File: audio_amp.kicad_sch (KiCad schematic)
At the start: 74 parts, among them IC115 RC4558, IC116 RC4558, IC117 RC4558, IC119 M51131L, IC120 CD4053B, P2 Conn_01x07_Male

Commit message: PCE expansion port added with only relevant pins.
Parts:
- removed #2: Conn_01x03_Female, symbol Connector:Conn_01x03_Female
- added #1, #5, L_#2, R_#2: Jumper_2_Bridged, symbol Jumper:Jumper_2_Bridged
- added C11: 100u, symbol Device:C_Polarized
- added C9: 100n, symbol Device:C
- added R120: 270, symbol Device:R
- added R35: 1k, symbol Device:R
- added R9: 75, symbol Device:R
- added SPC-E: PCE-EXPANSION-CONN, symbol IFU-30:PCE-EXPANSION-CONN
- added TR5: C2785, symbol Device:Q_NPN_ECB
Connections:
- net 7.9V: now also R120.1
- net GND: now also C11.2, C9.1, R9.2
- net PCE_AUDIO_LEFT: now also L_#2.1 (A), SPC-E.A0 (SNDL); no longer R14.1
- net PCE_AUDIO_RIGHT: now also R_#2.1 (A), SPC-E.C0 (SNDR); no longer R18.1
- net SPCE_B1_SNDIN renamed PCE_AUDIO_IN
- net PCE_AUDIO_IN: now also SPC-E.B0 (SNDIN)
- net VIDEO_IN: no longer names the net of C58.1
- net VIDEO_IN: now also #1.2 (B)
- new net: L_#2.2 (B), R14.1
- new net: #1.1 (A), R9.1, TR5.1 (E)
- new net: #5.1 (A), R120.2
- new net: R18.1, R_#2.2 (B)
- new net: #5.2 (B), C11.1, C9.2, TR5.2 (C)
- new net: R35.1, TR5.3 (B)
- new net PCE_VID: R35.2, SPC-E.A22 (VID)
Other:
- moved on the sheet: C12, C58, C8, IC117A, R104, R11, R15, R16, R21, R22, R33, R37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

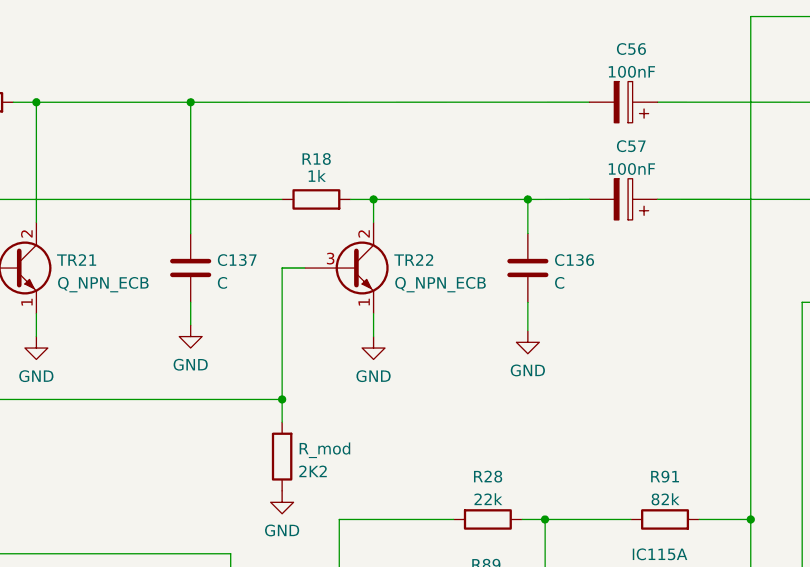
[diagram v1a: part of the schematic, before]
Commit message: Fixed mistake in ADPCM page and added notes about opamps.
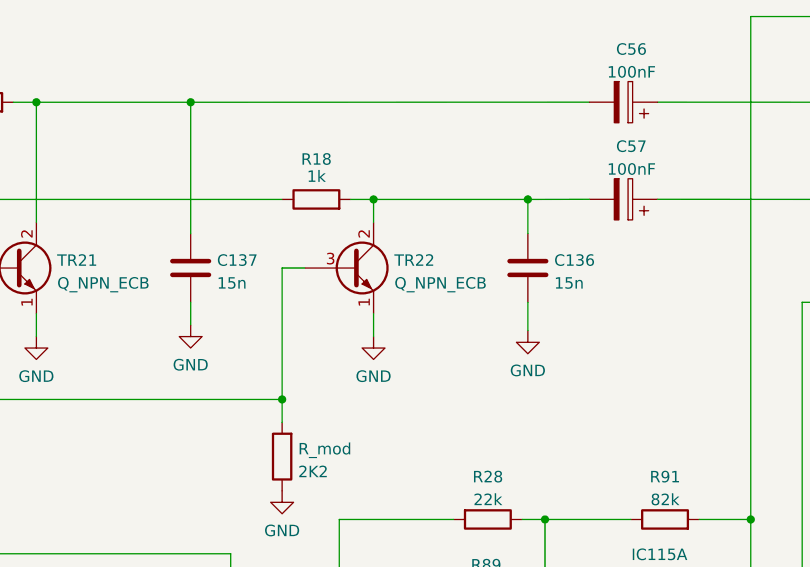
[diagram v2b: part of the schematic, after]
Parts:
- C136, C137: value C -> 15n
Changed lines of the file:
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@@
       (effects (font (size 1.27 1.27)) (justify left))
     )
-    (property "Value" "C" (id 1) (at 181.991 114.0972 0)
+    (property "Value" "15n" (id 1) (at 181.991 114.0972 0)
       (effects (font (size 1.27 1.27)) (justify left))
     )
@@
       (effects (font (size 1.27 1.27)) (justify left))
     )
-    (property "Value" "C" (id 1) (at 219.456 114.0972 0)
-      (effects (font (size 1.27 1.27)) (justify left))
-    )
+    (property "Value" "15n" (id 1) (at 219.456 114.0972 0)
+      (effects (font (size 1.27 1.27)) (justify left))
+    )

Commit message: All calculations added.
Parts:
- R91, R92: value 82k -> 8.2k
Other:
- note added: "text to paste into https://latex2png.com/ to have nice equations IC115A and B calculations At DC level \frac{V_{BIAS}/(15k+22k) + V_{BIAS}/28k + V_{IFU_R}/82k} {1/(15k+22k) + 1/28k + 1/8.2k}= V_{BIAS} \\ V_{BIAS}/37k + V_{BIAS}/28k + V_{IFU_R}/8.2k = V_{BIAS}/5.4144k \\ V_{IFU_R} = 3.95 \times (1/5.4144k - 1/37k - 1/28k) \times 8.2k \\ V_{IFU_R} = 3.95V V_{IFU_L} = 3.95V At AC level \frac{V_{CD_L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"
- note added: "text to paste into https://latex2png.com/ to have nice equations IC116A & IC116B calculations At DC level \frac{V_{IFUL}/R32 + V_{BIAS}/(R118+R31) + V_{AUDIOL}/R93}{1/R32 + 1/(R118+R31) + 1/R93} = V_{BIAS} \\ \frac{3.95/22k + 3.95/(15k+22k) + V_{AUDIOL}/62k} = 3.95 \times (1/22k + 1/(15k+22k) + 1/62) \\ V_{AUDIOL} = 62k \times 3.95 \times (1/11.285k - 1/22K - 1/37K) \\ V_{IFULR} = 3.95V At AC lev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"
- note added: "text to paste into https://latex2png.com/ to have nice equations V_{BIAS} = \frac{R20}{R20 + R19} \times (9V - V_{D1} - V_{TR2 BE}) \\ V_{BIAS} = \frac{10k}{10k + 10k} \times 7.9 \\ V_{BIAS} = 1/2 \times 7.9 \\ V_{BIAS} = 3.95V IC117A calculations At DC level \frac{V_{IFUL}/R16 + V_{IFUR}/R22 + V_{IFULR}/R21}{1/R16 + 1/R22 + 1/R21} = V_{BIAS} \\ \frac{3.95/33k + 3.95/33k + V_{IFULR}/39k}{1/33k + 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"
- note removed: "text to paste into https://latex2png.com/ to have nice equations V_{BIAS} = \frac{R20}{R20 + R19} \times (9V - V_{D1} - V_{TR2 BE}) \\ V_{BIAS} = \frac{10k}{10k + 10k} \times 7.9 \\ V_{BIAS} = 1/2 \times 7.9 \\ V_{BIAS} = 3.95V V_{BIAS} = \frac{V_{IFUL}/R16 + V_{IFUR}/R22 + V_{IFULR}/R21}{1/R16 + 1/R22 + 1/R21} 3.95 = \frac{V_{IFUL}/33k + V_{IFUR}/33K + V_{IFULR}/39K}{1/33k + 1/33k + 1/39k} 13.29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"
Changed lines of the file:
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@@
     (effects (font (size 1.27 1.27)) (justify left bottom))
   )
-  (text "text to paste into https://latex2png.com/ to have nice equations\n\nV_{BIAS} = \\frac{R20}{R20 + R19} \\times (9V - V_{D1} - V_{TR2 BE}) \\\\\nV_{BIAS} = \\frac{10k}{10k + 10k} \\times 7.9 \\\\\nV_{BIAS} = 1/2 \\times 7.9 \\\\\nV_{BIAS} = 3.95V\n\nV_{BIAS} = \\frac{V_{IFUL}/R16 + V_{IFUR}/R22 + V_{IFULR}/R21}{1/R16 + 1/R22 + 1/R21}\n\n3.95 = \\frac{V_{IFUL}/33k + V_{IFUR}/33K + V_{IFULR}/39K}{1/33k + 1/33k + 1/39k}\n\n13.29 = V_{IFUL} \\times 39k/33k + V_{IFUR} \\times 39k/33K + V_{IFULR}\n\nV_{IFULR} = 13.29 - V_{IFUR} \\times 39k/33K - V_{IFUR} \\times 39k/33K\n\nV_{IFULR} = 13.29 - V_{IFUR} \\times 1.18 - V_{IFUR} \\times 1.18\n\n\n"
-    (at 234.95 259.715 0)
+  (text "text to paste into https://latex2png.com/ to have nice equations\n\nV_{BIAS} = \\frac{R20}{R20 + R19} \\times (9V - V_{D1} - V_{TR2 BE}) \\\\\nV_{BIAS} = \\frac{10k}{10k + 10k} \\times 7.9 \\\\\nV_{BIAS} = 1/2 \\times 7.9 \\\\\nV_{BIAS} = 3.95V\n\nIC117A calculations\n\nAt DC level\n\\frac{V_{IFUL}/R16 + V_{IFUR}/R22 + V_{IFULR}/R21}{1/R16 + 1/R22 + 1/R21} = V_{BIAS} \\\\\n\\frac{3.95/33k + 3.95/33k + V_{IFULR}/39k}{1/33k + 1/33k + 1/39k} = 3.95 \\\\\nV_{IFULR} = 39k \\times 3.95 \\times (1/11.595k - 1/33K - 1/33K) \\\\\nV_{IFULR} = 3.95V\n\nAt AC level\n\\frac{V_{IFUL}/R16 + V_{IFUR}/R22 + V_{IFULR}/R21}{1/R16 + 1/R22 + 1/R21} = 0 \\\\\nV_{IFUL}/R16 + V_{IFUR}/R22 + V_{IFULR}/R21 = 0 \\\\\nV_{IFUL}/33k + V_{IFUR}/33k + V_{IFULR}/39k = 0 \\\\\nV_{IFULR} = - V_{IFUR} \\times 39/33 - V_{IFUR} \\times 39/33\n\nGain is 39/33 = 1.18"
+    (at 231.14 256.54 0)
     (effects (font (size 1.27 1.27)) (justify left bottom))
   )
@@
     (effects (font (size 1.27 1.27)) (justify left bottom))
   )
+  (text "text to paste into https://latex2png.com/ to have nice equations\n\nIC116A & IC116B calculations\n\nAt DC level\n\\frac{V_{IFUL}/R32 + V_{BIAS}/(R118+R31) + V_{AUDIOL}/R93}{1/R32 + 1/(R118+R31) + 1/R93} = V_{BIAS} \\\\\n\\frac{3.95/22k + 3.95/(15k+22k) + V_{AUDIOL}/62k} = 3.95 \\times (1/22k + 1/(15k+22k) + 1/62) \\\\\nV_{AUDIOL} = 62k \\times 3.95 \\times (1/11.285k - 1/22K - 1/37K) \\\\\nV_{IFULR} = 3.95V\n\nAt AC level\n\\frac{V_{IFUL}/R32 + V_{PCEL}/R31 + V_{AUDIOL}/R93}{1/R32 + 1/R31 + 1/R93} = 0 \\\\\nV_{IFUL}/R32 + V_{PCEL}/R31 + V_{AUDIOL}/R93 = 0 \\\\\nV_{AUDIOL} = - R93 \\times (V_{IFUL}/R32 + V_{PCEL}/R31) \\\\\nV_{AUDIOL} = - V_{IFUL} \\times 62/22 - V_{PCEL} \\times 62/22 \\\\\n\nGain is 62/22 = 2.818\n\nMultiplied by previous gain, we get 8.2/22 * 62/22 = 1.05 close enough to 1 (by 5%)"
+    (at 250.825 63.5 0)
+    (effects (font (size 1.27 1.27)) (justify left bottom))
+  )
   (text "Note on transistors:\nA1175 = PNP\nA144 = PNP (re-biased)\nC2001 = NPN\nAIL3Z = NPN\nC2785 = NPN\n\n"
-    (at 240.03 54.61 0)
+    (at 168.91 33.655 0)
     (effects (font (size 1.27 1.27)) (justify left bottom))
   )
   (text "With control (P12) connected to REF (5.2V),\nVolume 1 is applied to both left and right\n(simultaneous volume mode)\nVolume 2 is actually balance control but is fixed to Vref/2 which makes L and R volumes even."
     (at 44.45 219.075 0)
+    (effects (font (size 1.27 1.27)) (justify left bottom))
+  )
+  (text "text to paste into https://latex2png.com/ to have nice equations\n\nIC115A and B calculations\n\nAt DC level\n\\frac{V_{BIAS}/(15k+22k) + V_{BIAS}/28k + V_{IFU_R}/82k} {1/(15k+22k) + 1/28k + 1/8.2k}= V_{BIAS} \\\\\nV_{BIAS}/37k + V_{BIAS}/28k + V_{IFU_R}/8.2k = V_{BIAS}/5.4144k \\\\\nV_{IFU_R} = 3.95 \\times (1/5.4144k - 1/37k - 1/28k) \\times 8.2k \\\\\nV_{IFU_R} = 3.95V\n\nV_{IFU_L} = 3.95V\n\nAt AC level\n\\frac{V_{CD_L}/22k + V_{ADPCM}/28k + V_{FADE_L}/22k + V_{IFU_L}/8.2k}{1/22k + 1/28k + 1/22k + 1/8.2k} = 0 \\\\\nV_{IFU_L} = 8.2k \\times (-V_{CD_L}/22k - V_{ADPCM}/28k - V_{FADE_L}/22k) \\\\\nV_{IFU_L} = - V_{CD_L} \\times 8.2/22 - V_{ADPCM} \\times 8.2/28 - V_{FADE_L} \\times 8.2/22 \\\\\n\nV_{IFU_R} = - V_{CD_R} \\times 8.2/22 - V_{ADPCM} \\times 8.2/28 - V_{FADE_R} \\times 8.2/22 \\\\\n\nGain is 8.2/22 = 0.373"
+    (at 117.475 269.24 0)
     (effects (font (size 1.27 1.27)) (justify left bottom))
   )
@@
     (in_bom yes) (on_board yes) (fields_autoplaced)
     (property "Reference" "R91" (id 0) (at 231.775 135.6192 90))
-    (property "Value" "82k" (id 1) (at 231.775 138.1561 90))
+    (property "Value" "8.2k" (id 1) (at 231.775 138.1561 90))
     (property "Footprint" "" (id 2) (at 231.775 142.113 90)
       (effects (font (size 1.27 1.27)) hide)
@@
     (in_bom yes) (on_board yes) (fields_autoplaced)
     (property "Reference" "R92" (id 0) (at 229.235 168.0042 90))
-    (property "Value" "82k" (id 1) (at 229.235 170.5411 90))
+    (property "Value" "8.2k" (id 1) (at 229.235 170.5411 90))
     (property "Footprint" "" (id 2) (at 229.235 174.498 90)
       (effects (font (size 1.27 1.27)) hide)

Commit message: Documentation started.
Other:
- title: (none) -> NEC PC-Engine IFU-30
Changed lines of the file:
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@@
 (kicad_sch (version 20211123) (generator eeschema)
   (paper "A3")
+  (title_block
+    (title "NEC PC-Engine IFU-30")
+    (date "2022-10-27")
+    (rev "0.1")
+    (comment 1 "Author: Regis Galland")
+    (comment 2 "NEC IFU-30 PCB reverse engineered schematics")
+  )
   (junction (at 59.055 172.72) (diameter 0) (color 0 0 0 0)
   )
@@
     (effects (font (size 1.27 1.27)) (justify left bottom))
   )
-  (text "text to paste into https://latex2png.com/ to have nice equations\n\nIC115A and B calculations\n\nAt DC level\n\\frac{V_{BIAS}/(15k+22k) + V_{BIAS}/28k + V_{IFU_R}/82k} {1/(15k+22k) + 1/28k + 1/8.2k}= V_{BIAS} \\\\\nV_{BIAS}/37k + V_{BIAS}/28k + V_{IFU_R}/8.2k = V_{BIAS}/5.4144k \\\\\nV_{IFU_R} = 3.95 \\times (1/5.4144k - 1/37k - 1/28k) \\times 8.2k \\\\\nV_{IFU_R} = 3.95V\n\nV_{IFU_L} = 3.95V\n\nAt AC level\n\\frac{V_{CD_L}/22k + V_{ADPCM}/28k + V_{FADE_L}/22k + V_{IFU_L}/8.2k}{1/22k + 1/28k + 1/22k + 1/8.2k} = 0 \\\\\nV_{IFU_L} = 8.2k \\times (-V_{CD_L}/22k - V_{ADPCM}/28k - V_{FADE_L}/22k) \\\\\nV_{IFU_L} = - V_{CD_L} \\times 8.2/22 - V_{ADPCM} \\times 8.2/28 - V_{FADE_L} \\times 8.2/22 \\\\\n\nV_{IFU_R} = - V_{CD_R} \\times 8.2/22 - V_{ADPCM} \\times 8.2/28 - V_{FADE_R} \\times 8.2/22 \\\\\n\nGain is 8.2/22 = 0.373"
-    (at 117.475 269.24 0)
+  (text "text to paste into https://latex2png.com/ to have nice equations\n\nIC115A and B calculations\n\nAt DC level\n\\frac{V_{BIAS}/(15k+22k) + V_{BIAS}/28k + V_{IFU_R}/82k} {1/(15k+22k) + 1/28k + 1/8.2k}= V_{BIAS} \\\\\nV_{BIAS}/37k + V_{BIAS}/28k + V_{IFU_R}/8.2k = V_{BIAS}/5.4144k \\\\\nV_{IFU_R} = 3.95 \\times (1/5.4144k - 1/37k - 1/28k) \\times 8.2k \\\\\nV_{IFU_R} = 3.95V\n\nV_{IFU_L} = 3.95V\n\nAt AC level\n\\frac{V_{CD_L}/22k + V_{ADPCM}/28k + V_{FADE_L}/22k + V_{IFU_L}/8.2k}{1/22k + 1/28k + 1/22k + 1/8.2k} = 0 \\\\\nV_{IFU_L} = 8.2k \\times (-V_{CD_L}/22k - V_{ADPCM}/28k - V_{FADE_L}/22k) \\\\\nV_{IFU_L} = - V_{CD_L} \\times 8.2/22 - V_{ADPCM} \\times 8.2/28 - V_{FADE_L} \\times 8.2/22 \\\\\n\nV_{IFU_R} = - V_{CD_R} \\times 8.2/22 - V_{ADPCM} \\times 8.2/28 - V_{FADE_R} \\times 8.2/22 \\\\\n\nGain is 8.2/22 = 0.373 for CD and 8.2/28 = 0.293 for ADPCM\n\nM51131 Inputs have a 150kohm resistance. This explains why ADPCM goes through 47k to maintain the \n22/28 ratio when cd and adpcm signal are fed directly to IC115 as 22/28 = 150/147.  "
+    (at 113.665 277.495 0)
     (effects (font (size 1.27 1.27)) (justify left bottom))
   )

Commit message: Documentation update
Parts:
- removed IC120: CD4053B, symbol Analog_Switch:CD4053B
- added IC120: 4053, symbol 4xxx:4053
- R27, R29: value 28k -> 27k
- renumbered R_mod to R999, SPC-E to SPC-E1
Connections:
- net ADPCM_OUT: now also IC120.4 (Z)
- net FADE_~{SEL}: now also IC120.10 (B), IC120.11 (A), IC120.9 (C)
- net GND: now also IC120.6 (Inh), IC120.7 (VEE), IC120.8 (VSS)
- net at C19.1, R53.1: now also IC120.14 (X)
- net at R44.2, R45.1, R46.2: now also IC120.3 (Z1)
- net at R27.2, R29.1: now also IC120.5 (Z0)
- net at R30.1: now also IC120.1 (Y1)
- net at C17.1, R45.2: now also IC120.12 (X0)
- net at R28.2: now also IC120.13 (X1)
- net at C20.1, R52.1: now also IC120.15 (Y)
- net at C18.1, R46.1: now also IC120.2 (Y0)
- net 7.9V renamed 7.8V
- net 7.8V: now also IC120.16 (VDD)
- net VBIAS_3.95V renamed VBIAS_3.9V
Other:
- note removed: "Note on transistors: A1175 = PNP A144 = PNP (re-biased) C2001 = NPN AIL3Z = NPN C2785 = NPN"
- note removed: "text to paste into https://latex2png.com/ to have nice equations IC115A and B calculations At DC level \frac{V_{BIAS}/(15k+22k) + V_{BIAS}/28k + V_{IFU_R}/82k} {1/(15k+22k) + 1/28k + 1/8.2k}= V_{BIAS} \\ V_{BIAS}/37k + V_{BIAS}/28k + V_{IFU_R}/8.2k = V_{BIAS}/5.4144k \\ V_{IFU_R} = 3.95 \times (1/5.4144k - 1/37k - 1/28k) \times 8.2k \\ V_{IFU_R} = 3.95V V_{IFU_L} = 3.95V At AC level \frac{V_{CD_L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"
- moved on the sheet: C19, C20, R44, R52, R53, R82, R83

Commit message: Fixed a few typos and mainly renamed connections to CD-ROM with more accurate descriptions
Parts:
- P2: value Conn_01x07_Male -> Conn_01x07_Pin; symbol Connector:Conn_01x07_Male -> Connector:Conn_01x07_Pin
- SPC-E1: footprint (none) -> IFU-30:PinSocket_3x23_P2.54mm_Horizontal
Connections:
- net PCE_AUDIO_IN: now also SPC-E1.B01 (SNDIN); no longer SPC-E1.B0 (SNDIN)
- net PCE_AUDIO_LEFT: now also SPC-E1.A01 (SNDL); no longer SPC-E1.A0 (SNDL)
- net PCE_AUDIO_RIGHT: now also SPC-E1.C01 (SNDR); no longer SPC-E1.C0 (SNDR)
- net PCE_VID: now also SPC-E1.A23 (VID); no longer SPC-E1.A22 (VID)
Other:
- note added: "R999 is an external mod on my PCB"
- moved on the sheet: C10, C11, C12, C13, C136, C137, C14, C16, C4, C57, C58, C8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
